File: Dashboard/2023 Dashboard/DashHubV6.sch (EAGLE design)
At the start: 33 parts, among them J1 LEFT, J2 RIGHT, U1 ALLEGRO_MICROSYSTEMS_ACS722LL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, U2 XBEE_PRO_S3B

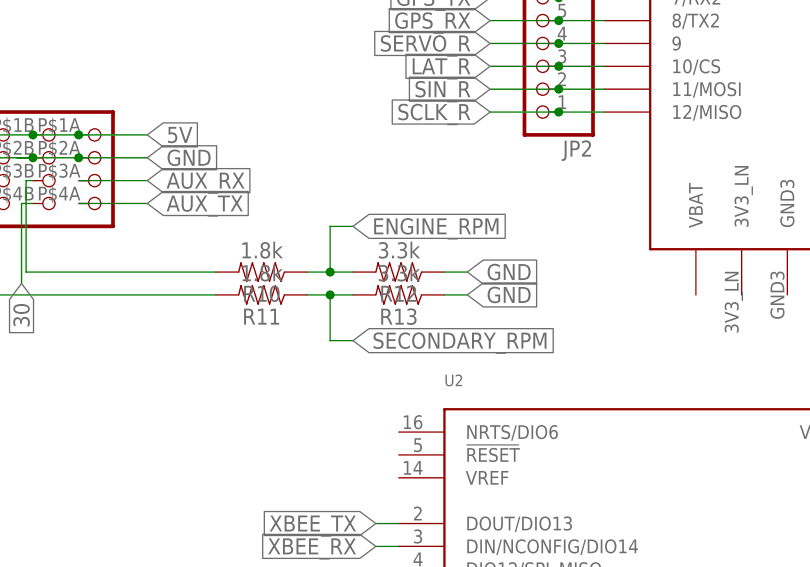
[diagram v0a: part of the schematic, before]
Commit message: Updated pull ups on dashboard
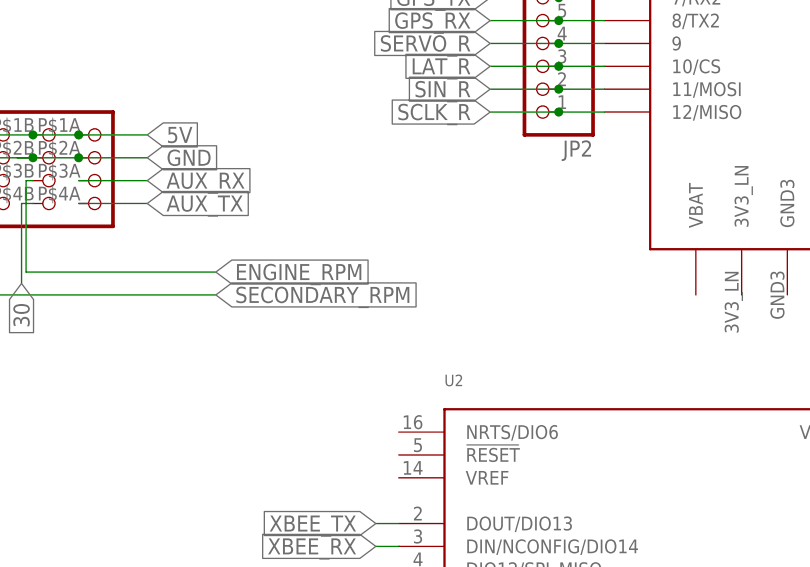
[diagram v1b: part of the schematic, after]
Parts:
- removed R10, R11: 1.8k, SparkFun-Resistors:RESISTORAXIAL-0.3
- removed R12, R13: 3.3k, SparkFun-Resistors:RESISTORAXIAL-0.3
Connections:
- removed net N$23: R10.2, U$4.3B
- removed net N$24: R11.2, U$4.3C
- net ENGINE_RPM: now also U$4.3B; no longer R10.1, R12.2
- net GND: no longer R12.1, R13.1
- net SECONDARY_RPM: now also U$4.3C; no longer R11.1, R13.2
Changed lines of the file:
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@@
 <part name="JP2" library="pinhead" library_urn="urn:adsk.eagle:library:325" deviceset="PINHD-1X14" device="" package3d_urn="urn:adsk.eagle:package:22417/2"/>
 <part name="JP3" library="pinhead" library_urn="urn:adsk.eagle:library:325" deviceset="PINHD-1X14" device="" package3d_urn="urn:adsk.eagle:package:22417/2"/>
-<part name="R10" library="SparkFun-Resistors" library_urn="urn:adsk.eagle:library:532" deviceset="RESISTOR" device="AXIAL-0.3" package3d_urn="urn:adsk.eagle:package:39658/1" value="1.8k"/>
-<part name="R11" library="SparkFun-Resistors" library_urn="urn:adsk.eagle:library:532" deviceset="RESISTOR" device="AXIAL-0.3" package3d_urn="urn:adsk.eagle:package:39658/1" value="1.8k"/>
-<part name="R12" library="SparkFun-Resistors" library_urn="urn:adsk.eagle:library:532" deviceset="RESISTOR" device="AXIAL-0.3" package3d_urn="urn:adsk.eagle:package:39658/1" value="3.3k"/>
-<part name="R13" library="SparkFun-Resistors" library_urn="urn:adsk.eagle:library:532" deviceset="RESISTOR" device="AXIAL-0.3" package3d_urn="urn:adsk.eagle:package:39658/1" value="3.3k"/>
 <part name="JP4" library="pinhead" library_urn="urn:adsk.eagle:library:325" deviceset="PINHD-2X5" device="" package3d_urn="urn:adsk.eagle:package:22470/2"/>
 <part name="LED1" library="led" library_urn="urn:adsk.eagle:library:259" deviceset="LED" device="CHIPLED_1206" package3d_urn="urn:adsk.eagle:package:15823/2"/>
@@
 <attribute name="VALUE" x="176.53" y="43.18" size="1.778" layer="96"/>
 </instance>
-<instance part="R10" gate="G$1" x="96.52" y="30.48" smashed="yes" rot="R180">
-<attribute name="NAME" x="96.52" y="28.956" size="1.778" layer="95" font="vector" rot="R180" align="bottom-center"/>
-<attribute name="VALUE" x="96.52" y="32.004" size="1.778" layer="96" font="vector" rot="R180" align="top-center"/>
-</instance>
-<instance part="R11" gate="G$1" x="96.52" y="27.94" smashed="yes" rot="R180">
-<attribute name="NAME" x="96.52" y="26.416" size="1.778" layer="95" font="vector" rot="R180" align="bottom-center"/>
-<attribute name="VALUE" x="96.52" y="29.464" size="1.778" layer="96" font="vector" rot="R180" align="top-center"/>
-</instance>
-<instance part="R12" gate="G$1" x="111.76" y="30.48" smashed="yes" rot="R180">
-<attribute name="NAME" x="111.76" y="28.956" size="1.778" layer="95" font="vector" rot="R180" align="bottom-center"/>
-<attribute name="VALUE" x="111.76" y="32.004" size="1.778" layer="96" font="vector" rot="R180" align="top-center"/>
-</instance>
-<instance part="R13" gate="G$1" x="111.76" y="27.94" smashed="yes" rot="R180">
-<attribute name="NAME" x="111.76" y="26.416" size="1.778" layer="95" font="vector" rot="R180" align="bottom-center"/>
-<attribute name="VALUE" x="111.76" y="29.464" size="1.778" layer="96" font="vector" rot="R180" align="top-center"/>
-</instance>
 <instance part="JP4" gate="A" x="142.24" y="111.76" smashed="yes">
 <attribute name="NAME" x="135.89" y="120.015" size="1.778" layer="95"/>
@@
 <wire x1="53.34" y1="96.52" x2="55.88" y2="96.52" width="0.1524" layer="91"/>
 <label x="55.88" y="96.52" size="1.778" layer="95" xref="yes"/>
-</segment>
-<segment>
-<pinref part="R12" gate="G$1" pin="1"/>
-<wire x1="116.84" y1="30.48" x2="119.38" y2="30.48" width="0.1524" layer="91"/>
-<label x="119.38" y="30.48" size="1.778" layer="95" xref="yes"/>
-</segment>
-<segment>
-<pinref part="R13" gate="G$1" pin="1"/>
-<wire x1="116.84" y1="27.94" x2="119.38" y2="27.94" width="0.1524" layer="91"/>
-<label x="119.38" y="27.94" size="1.778" layer="95" xref="yes"/>
 </segment>
 <segment>
@@
 <net name="ENGINE_RPM" class="0">
 <segment>
-<pinref part="R10" gate="G$1" pin="1"/>
-<pinref part="R12" gate="G$1" pin="2"/>
-<wire x1="101.6" y1="30.48" x2="104.14" y2="30.48" width="0.1524" layer="91"/>
-<wire x1="104.14" y1="30.48" x2="106.68" y2="30.48" width="0.1524" layer="91"/>
-<junction x="104.14" y="30.48"/>
-<wire x1="104.14" y1="30.48" x2="104.14" y2="35.56" width="0.1524" layer="91"/>
-<wire x1="104.14" y1="35.56" x2="106.68" y2="35.56" width="0.1524" layer="91"/>
-<label x="106.68" y="35.56" size="1.778" layer="95" xref="yes"/>
-</segment>
-<segment>
 <pinref part="U$1" gate="G$1" pin="22/A8"/>
 <pinref part="JP3" gate="A" pin="5"/>
@@
 <label x="187.96" y="71.12" size="1.778" layer="95" xref="yes"/>
 </segment>
+<segment>
+<wire x1="70.358" y1="30.48" x2="91.44" y2="30.48" width="0.1524" layer="91"/>
+<wire x1="71.12" y1="40.64" x2="70.358" y2="40.64" width="0.1524" layer="91"/>
+<wire x1="70.358" y1="40.64" x2="70.358" y2="30.48" width="0.1524" layer="91"/>
+<pinref part="U$4" gate="G$1" pin="3B"/>
+<label x="91.44" y="30.48" size="1.778" layer="95" xref="yes"/>
+</segment>
 </net>
 <net name="AUX_TX" class="0">
@@
 <net name="SECONDARY_RPM" class="0">
 <segment>
-<pinref part="R11" gate="G$1" pin="1"/>
-<pinref part="R13" gate="G$1" pin="2"/>
-<wire x1="101.6" y1="27.94" x2="104.14" y2="27.94" width="0.1524" layer="91"/>
-<wire x1="104.14" y1="27.94" x2="106.68" y2="27.94" width="0.1524" layer="91"/>
-<junction x="104.14" y="27.94"/>
-<wire x1="104.14" y1="27.94" x2="104.14" y2="22.86" width="0.1524" layer="91"/>
-<wire x1="104.14" y1="22.86" x2="106.68" y2="22.86" width="0.1524" layer="91"/>
-<label x="106.68" y="22.86" size="1.778" layer="95" xref="yes"/>
-</segment>
-<segment>
 <pinref part="U$1" gate="G$1" pin="23/A9"/>
 <pinref part="JP3" gate="A" pin="4"/>
@@
 <label x="187.96" y="73.66" size="1.778" layer="95" xref="yes"/>
 </segment>
+<segment>
+<wire x1="65.024" y1="27.94" x2="91.44" y2="27.94" width="0.1524" layer="91"/>
+<pinref part="U$4" gate="G$1" pin="3C"/>
+<wire x1="66.04" y1="40.64" x2="65.024" y2="40.64" width="0.1524" layer="91"/>
+<wire x1="65.024" y1="40.64" x2="65.024" y2="27.94" width="0.1524" layer="91"/>
+<label x="91.44" y="27.94" size="1.778" layer="95" xref="yes"/>
+</segment>
 </net>
 <net name="SIN_R" class="0">
@@
 </segment>
 </net>
-<net name="N$23" class="0">
-<segment>
-<pinref part="R10" gate="G$1" pin="2"/>
-<wire x1="70.358" y1="30.48" x2="91.44" y2="30.48" width="0.1524" layer="91"/>
-<wire x1="71.12" y1="40.64" x2="70.358" y2="40.64" width="0.1524" layer="91"/>
-<wire x1="70.358" y1="40.64" x2="70.358" y2="30.48" width="0.1524" layer="91"/>
-<pinref part="U$4" gate="G$1" pin="3B"/>
-</segment>
-</net>
-<net name="N$24" class="0">
-<segment>
-<wire x1="65.024" y1="27.94" x2="91.44" y2="27.94" width="0.1524" layer="91"/>
-<pinref part="R11" gate="G$1" pin="2"/>
-<pinref part="U$4" gate="G$1" pin="3C"/>
-<wire x1="66.04" y1="40.64" x2="65.024" y2="40.64" width="0.1524" layer="91"/>
-<wire x1="65.024" y1="40.64" x2="65.024" y2="27.94" width="0.1524" layer="91"/>
-</segment>
-</net>

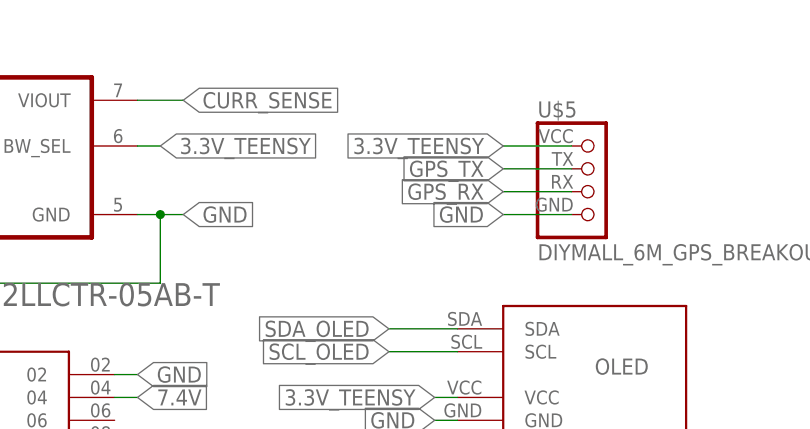
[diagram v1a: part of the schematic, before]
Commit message: Updated dash hub to power GPS with 5V
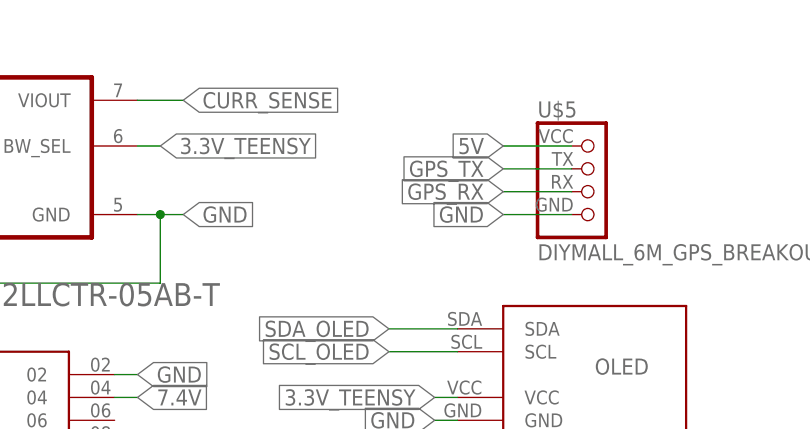
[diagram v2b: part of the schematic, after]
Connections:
- net 3.3V_TEENSY: no longer U$5.VCC
- net 5V: now also U$5.VCC
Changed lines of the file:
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@@
-</segment>
-<segment>
-<pinref part="U$5" gate="G$1" pin="VCC"/>
-<wire x1="104.14" y1="121.92" x2="96.52" y2="121.92" width="0.1524" layer="91"/>
-<label x="96.52" y="121.92" size="1.778" layer="95" rot="R180" xref="yes"/>
 </segment>
 <segment>
@@
 <junction x="76.2" y="45.72"/>
 </segment>
+<segment>
+<pinref part="U$5" gate="G$1" pin="VCC"/>
+<wire x1="104.14" y1="121.92" x2="96.52" y2="121.92" width="0.1524" layer="91"/>
+<label x="96.52" y="121.92" size="1.778" layer="95" rot="R180" xref="yes"/>
+</segment>
 </net>

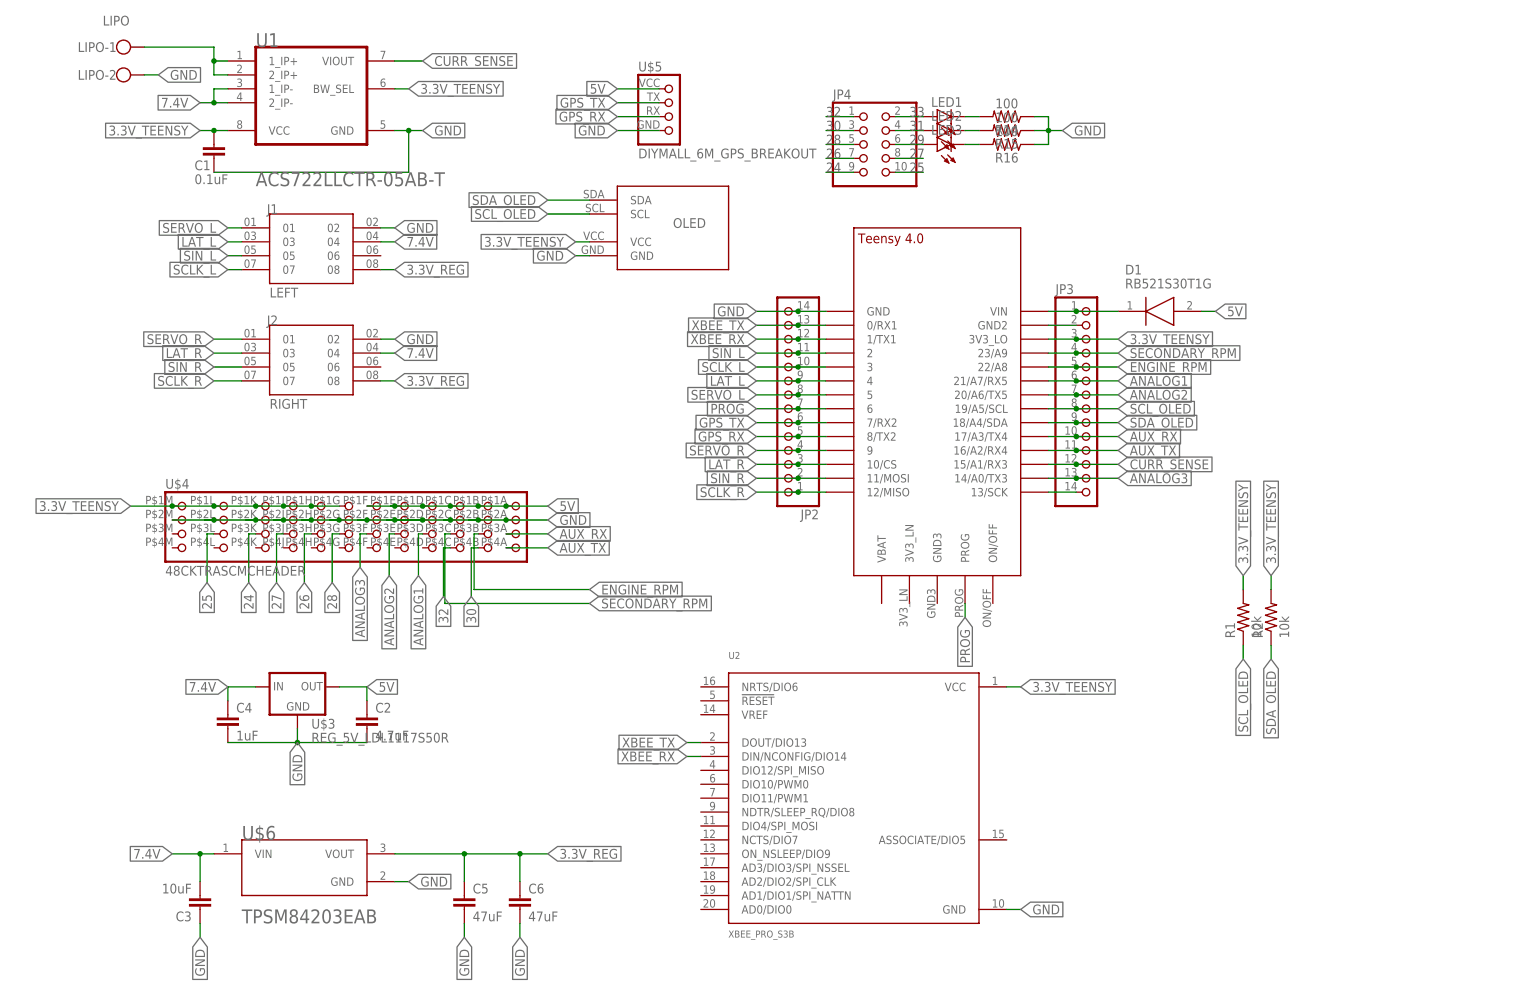
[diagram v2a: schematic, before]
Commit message: Update dashboard pcb files
Removed xbee and current sensor
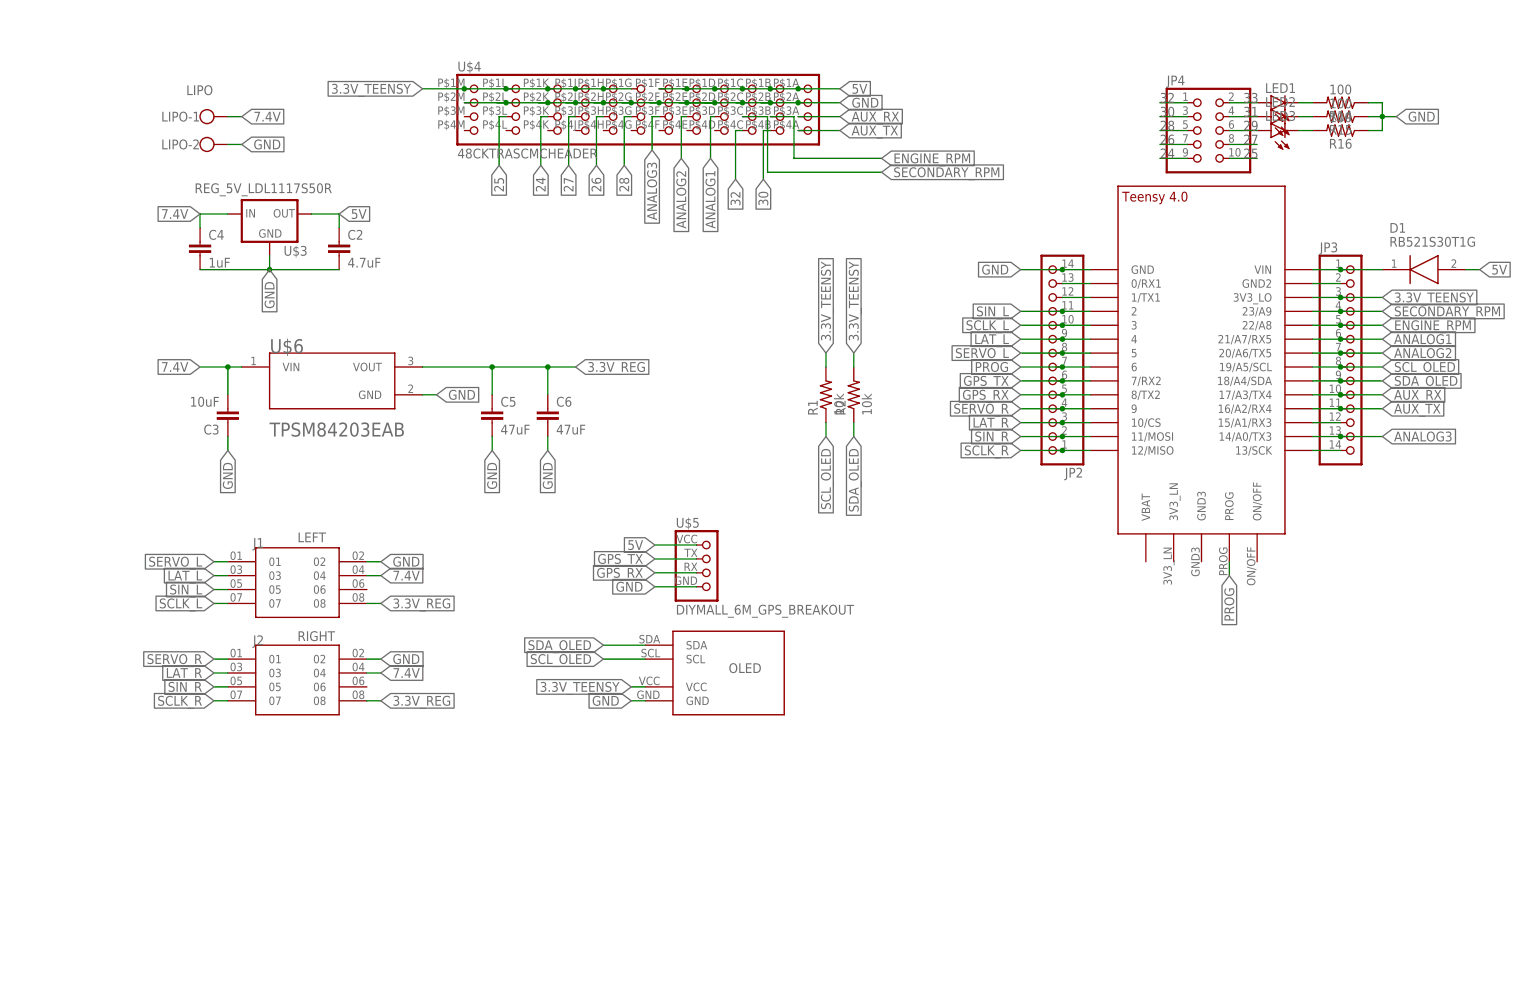
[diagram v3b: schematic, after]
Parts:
- removed C1: 0.1uF, rcl:C-EUC0402
- removed U1: ALLEGRO_MICROSYSTEMS_ACS722LLCTR-05AB-TALLEGRO_MICROSYSTEMS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, Allegro MicroSystems - ACS722LLCTR-05AB-T:ALLEGRO_MICROSYSTEMS_ACS722LLCTR-05AB-TALLEGRO_MICROSYSTEMS_ACS722LLCTR-05AB-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
- removed U2: XBEE_PRO_S3B, GTOR - Microcontroller:XBEE_PRO_S3B
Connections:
- removed net LIPO_IN: LIPO-1.KL, U1.1_IP+, U1.2_IP+
- net 3.3V_TEENSY: no longer C1.2, U1.BW_SEL, U1.VCC, U2.VCC
- net 7.4V: now also LIPO-1.KL; no longer U1.1_IP-, U1.2_IP-
- net CURR_SENSE: no longer U1.VIOUT
- net GND: no longer C1.1, U1.GND, U2.GND
- net XBEE_RX: no longer U2.DIN/NCONFIG/DIO14
- net XBEE_TX: no longer U2.DOUT/DIO13
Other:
- moved on the sheet: C2, C3, C4, C5, C6, D1, J1, J2, JP2, JP3, JP4, LED1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
